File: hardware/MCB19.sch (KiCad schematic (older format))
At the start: 1 part

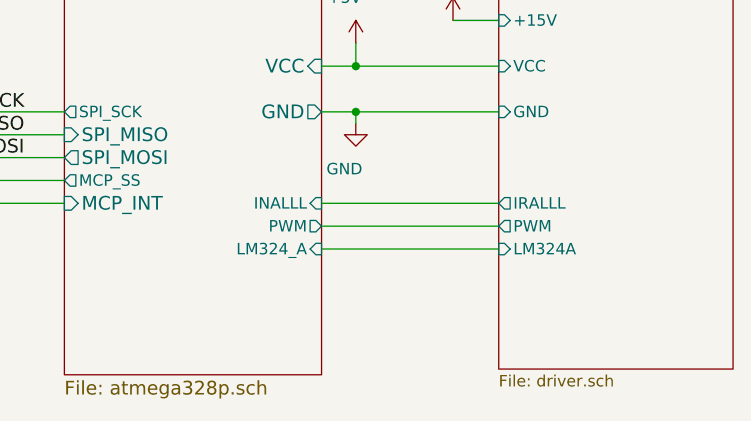
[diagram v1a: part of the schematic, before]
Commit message: Adição das mudanças pré-DSB(SF) feitas no MCB19
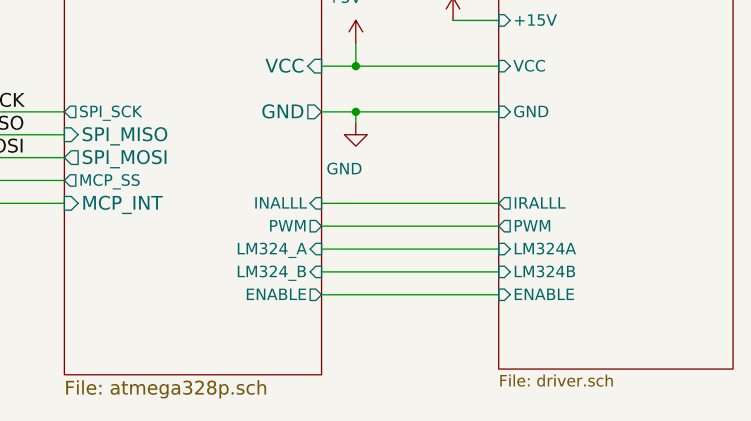
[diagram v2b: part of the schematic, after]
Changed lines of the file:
@@
 EESchema Schematic File Version 4
-EELAYER 30 0
+EELAYER 26 0
 EELAYER END
 $Descr A4 11693 8268
@@
 F10 "PWM" O R 7125 4700 50
 F11 "LM324_A" I R 7125 4800 50
+F12 "LM324_B" I R 7125 4900 50
+F13 "ENABLE" O R 7125 5000 50
 $EndSheet
 $Sheet
@@
 F6 "LM324A" I L 7900 4800 50
 F7 "+15V" I L 7900 3800 50
+F8 "ENABLE" I L 7900 5000 50
+F9 "LM324B" I L 7900 4900 50
 $EndSheet
 Wire Wire Line
@@
 F4 "+18V_IN" I L 4500 3100 50
 $EndSheet
+Wire Wire Line
+	7900 4900 7125 4900
+Wire Wire Line
+	7125 5000 7900 5000
 $EndSCHEMATC

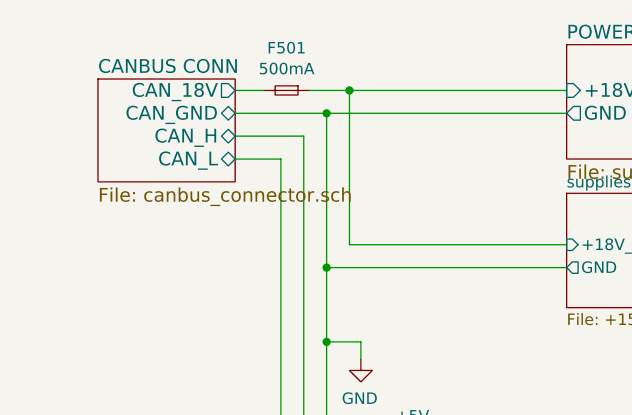
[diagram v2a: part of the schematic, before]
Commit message: small fixes in layout. Fabrication files exported.
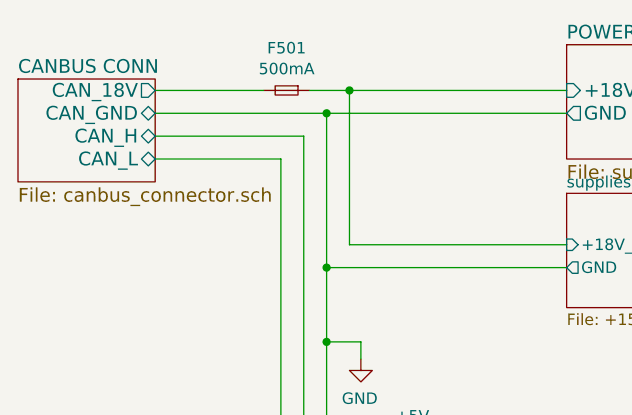
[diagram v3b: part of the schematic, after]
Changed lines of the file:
@@
 EESchema Schematic File Version 4
-EELAYER 26 0
+EELAYER 30 0
 EELAYER END
 $Descr A4 11693 8268
@@
 $EndSheet
 $Sheet
-S 2450 2375 600  450
+S 2100 2375 600  450
 U 5AAD16DD
 F0 "CANBUS CONN" 60
 F1 "canbus_connector.sch" 60
-F2 "CAN_H" B R 3050 2625 60
-F3 "CAN_L" B R 3050 2725 60
-F4 "CAN_18V" O R 3050 2425 60
-F5 "CAN_GND" B R 3050 2525 60
+F2 "CAN_H" B R 2700 2625 60
+F3 "CAN_L" B R 2700 2725 60
+F4 "CAN_18V" O R 2700 2425 60
+F5 "CAN_GND" B R 2700 2525 60
 $EndSheet
 Text Label 5825 4400 2    60   ~ 0
@@
 SCK
 Wire Wire Line
-	3050 2625 3350 2625
+	2700 2625 3350 2625
 Wire Wire Line
 	4075 4450 3250 4450
 Wire Wire Line
-	3250 2725 3050 2725
+	3250 2725 2700 2725
 Wire Wire Line
 	5550 2525 5750 2525
@@
 	3875 4150 4075 4150
 Wire Wire Line
-	3450 2525 3050 2525
+	3450 2525 2700 2525
 $Comp
 L power:+5V #PWR0105
@@
 $EndComp
 Wire Wire Line
-	3175 2425 3050 2425
+	3175 2425 2700 2425
 Wire Wire Line
 	6000 4200 5425 4200

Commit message: driver better referenced to low-side mosfet
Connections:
- net labels added: +12V
- net labels removed: +15V
- wire segments 41 -> 42
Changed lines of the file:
@@
 L power:GND #PWR0103
 U 1 1 5CDE058E
-P 3600 3600
-F 0 "#PWR0103" H 3600 3350 50  0001 C CNN
-F 1 "GND" H 3605 3427 50  0000 C CNN
-F 2 "" H 3600 3600 50  0001 C CNN
-F 3 "" H 3600 3600 50  0001 C CNN
-	1    3600 3600
+P 3650 3600
+F 0 "#PWR0103" H 3650 3350 50  0001 C CNN
+F 1 "GND" H 3655 3427 50  0000 C CNN
+F 2 "" H 3650 3600 50  0001 C CNN
+F 3 "" H 3650 3600 50  0001 C CNN
+	1    3650 3600
 	-1   0    0    -1
 $EndComp
 Wire Wire Line
-	3600 3600 3600 3525
+	3650 3600 3650 3525
 Wire Wire Line
-	3600 3525 3450 3525
+	3650 3525 3450 3525
 Wire Wire Line
 	3875 4050 3875 4150
@@
 F5 "PWM" O L 7900 4700 50
 F6 "LM324A" I L 7900 4800 50
-F7 "+15V" I L 7900 3800 50
+F7 "+12V" I L 7900 3800 50
 F8 "ENABLE" I L 7900 5000 50
 F9 "LM324B" I L 7900 4900 50
+F10 "ENABLE_RELAY" I L 7900 5000 50
 $EndSheet
 Wire Wire Line
@@
 	3550 2425 3375 2425
 $Comp
-L power:+15V #PWR0109
+L power:+12V #PWR0109
 U 1 1 5D9C5743
 P 5750 3200
 F 0 "#PWR0109" H 5750 3050 50  0001 C CNN
-F 1 "+15V" H 5765 3373 50  0000 C CNN
+F 1 "+12V" H 5765 3373 50  0000 C CNN
 F 2 "" H 5750 3200 50  0001 C CNN
 F 3 "" H 5750 3200 50  0001 C CNN
@@
 	5550 3200 5750 3200
 $Comp
-L power:+15V #PWR0112
+L power:+12V #PWR0112
 U 1 1 5DA06051
 P 7700 3800
 F 0 "#PWR0112" H 7700 3650 50  0001 C CNN
-F 1 "+15V" H 7715 3973 50  0000 C CNN
+F 1 "+12V" H 7715 3973 50  0000 C CNN
 F 2 "" H 7700 3800 50  0001 C CNN
 F 3 "" H 7700 3800 50  0001 C CNN
@@
 S 4500 2875 1050 500
 U 5DA09AB7
-F0 "supplies15" 50
-F1 "+15V.sch" 50
+F0 "supplies12" 50
+F1 "+12V.sch" 50
 F2 "GND" O L 4500 3200 50
-F3 "+15V_OUT" I R 5550 3200 50
+F3 "+12V_OUT" I R 5550 3200 50
 F4 "+18V_IN" I L 4500 3100 50
 $EndSheet
@@
 Wire Wire Line
 	7125 5000 7900 5000
+$Comp
+L power:PWR_FLAG #FLG0102
+U 1 1 5E3CC6C1
+P 3650 3450
+F 0 "#FLG0102" H 3650 3525 50  0001 C CNN
+F 1 "PWR_FLAG" H 3675 3650 50  0000 C CNN
+F 2 "" H 3650 3450 50  0001 C CNN
+F 3 "~" H 3650 3450 50  0001 C CNN
+	1    3650 3450
+	1    0    0    -1
+$EndComp
+Connection ~ 3650 3525
+Wire Wire Line
+	3650 3525 3650 3450
 $EndSCHEMATC

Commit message: relay finished
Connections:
- net labels added: VCC
- wire segments 42 -> 46
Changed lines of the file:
@@
 $EndComp
-Wire Wire Line
-	3175 2425 2700 2425
 Wire Wire Line
 	6000 4200 5425 4200
@@
 F13 "ENABLE" O R 7125 5000 50
 $EndSheet
-$Sheet
-S 7900 3700 1025 1625
-U 5D414D87
-F0 "driver" 50
-F1 "driver.sch" 50
-F2 "VCC" I L 7900 4000 50
-F3 "GND" I L 7900 4200 50
-F4 "IRALLL" O L 7900 4600 50
-F5 "PWM" O L 7900 4700 50
-F6 "LM324A" I L 7900 4800 50
-F7 "+12V" I L 7900 3800 50
-F8 "ENABLE" I L 7900 5000 50
-F9 "LM324B" I L 7900 4900 50
-F10 "ENABLE_RELAY" I L 7900 5000 50
-$EndSheet
 Wire Wire Line
 	3450 2525 3450 3200
 Wire Wire Line
-	4500 2425 3550 2425
+	4500 2425 3775 2425
 Wire Wire Line
 	7900 4600 7125 4600
@@
 Wire Wire Line
 	5550 3200 5750 3200
-$Comp
-L power:+12V #PWR0112
-U 1 1 5DA06051
-P 7700 3800
-F 0 "#PWR0112" H 7700 3650 50  0001 C CNN
-F 1 "+12V" H 7715 3973 50  0000 C CNN
-F 2 "" H 7700 3800 50  0001 C CNN
-F 3 "" H 7700 3800 50  0001 C CNN
-	1    7700 3800
-	1    0    0    -1
-$EndComp
-Wire Wire Line
-	7700 3800 7900 3800
 $Sheet
 S 4500 2875 1050 500
@@
 Wire Wire Line
 	3650 3525 3650 3450
+$Comp
+L power:VCC #PWR0119
+U 1 1 5E262F9D
+P 3775 2100
+F 0 "#PWR0119" H 3775 1950 50  0001 C CNN
+F 1 "VCC" H 3792 2273 50  0000 C CNN
+F 2 "" H 3775 2100 50  0001 C CNN
+F 3 "" H 3775 2100 50  0001 C CNN
+	1    3775 2100
+	1    0    0    -1
+$EndComp
+$Comp
+L power:VCC #PWR0120
+U 1 1 5E26394F
+P 7825 3650
+F 0 "#PWR0120" H 7825 3500 50  0001 C CNN
+F 1 "VCC" H 7842 3823 50  0000 C CNN
+F 2 "" H 7825 3650 50  0001 C CNN
+F 3 "" H 7825 3650 50  0001 C CNN
+	1    7825 3650
+	1    0    0    -1
+$EndComp
+Wire Wire Line
+	7700 3900 7900 3900
+$Comp
+L power:+12V #PWR0112
+U 1 1 5DA06051
+P 7700 3900
+F 0 "#PWR0112" H 7700 3750 50  0001 C CNN
+F 1 "+12V" H 7715 4073 50  0000 C CNN
+F 2 "" H 7700 3900 50  0001 C CNN
+F 3 "" H 7700 3900 50  0001 C CNN
+	1    7700 3900
+	1    0    0    -1
+$EndComp
+$Sheet
+S 7900 3700 1025 1625
+U 5D414D87
+F0 "driver" 50
+F1 "driver.sch" 50
+F2 "VCC" I L 7900 4000 50
+F3 "GND" I L 7900 4200 50
+F4 "IRALLL" O L 7900 4600 50
+F5 "PWM" O L 7900 4700 50
+F6 "LM324A" I L 7900 4800 50
+F7 "+12V" I L 7900 3900 50
+F8 "ENABLE" I L 7900 5000 50
+F9 "LM324B" I L 7900 4900 50
+F10 "ENABLE_RELAY" I L 7900 5000 50
+F11 "+18V" I L 7900 3800 50
+$EndSheet
+Wire Wire Line
+	7825 3800 7900 3800
+Wire Wire Line
+	7825 3650 7825 3800
+Wire Wire Line
+	2700 2425 3175 2425
+Wire Wire Line
+	3775 2100 3775 2425
+Connection ~ 3775 2425
+Wire Wire Line
+	3775 2425 3550 2425
 $EndSCHEMATC

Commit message: Some fixes, ready for heat transfering
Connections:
- wire segments 46 -> 47
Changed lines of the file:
@@
 	3450 2525 3450 3200
 Wire Wire Line
-	4500 2425 3775 2425
+	4500 2425 4025 2425
 Wire Wire Line
 	7900 4600 7125 4600
@@
 Wire Wire Line
 	3775 2425 3550 2425
+$Comp
+L power:PWR_FLAG #FLG0104
+U 1 1 5E9A1334
+P 4025 2425
+F 0 "#FLG0104" H 4025 2500 50  0001 C CNN
+F 1 "PWR_FLAG" H 4050 2625 50  0000 C CNN
+F 2 "" H 4025 2425 50  0001 C CNN
+F 3 "~" H 4025 2425 50  0001 C CNN
+	1    4025 2425
+	1    0    0    -1
+$EndComp
+Connection ~ 4025 2425
+Wire Wire Line
+	4025 2425 3775 2425
 $EndSCHEMATC
